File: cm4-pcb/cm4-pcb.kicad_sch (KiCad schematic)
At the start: 34 parts, among them J1 Conn_01x02_Pin, J2 Conn_01x02_Pin, J3 USB1125-GF-B, J4 Conn_02x03_Odd_Even, J5 Conn_01x04, J6 J0011D21NL, J7 Conn_01x02, U1 Pfostenstecker_6_2x3, U2 Pfostenstecker_6_2x3, U5 SMD-PUSH-BTN

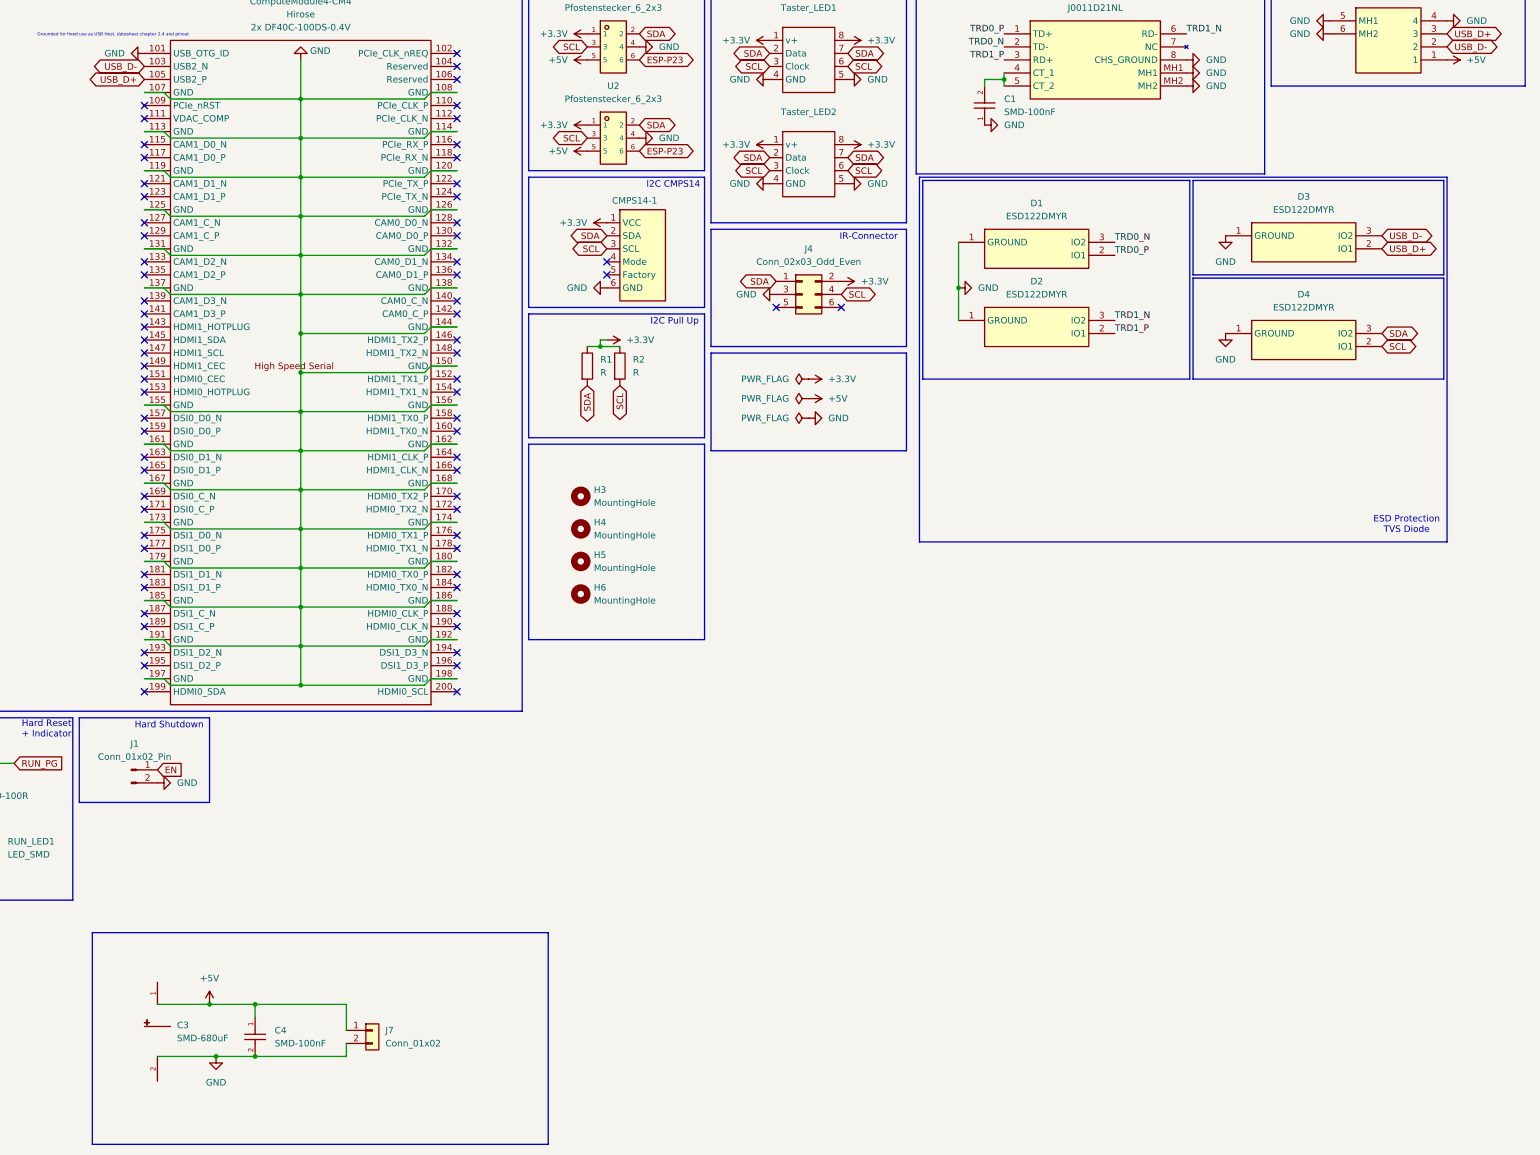
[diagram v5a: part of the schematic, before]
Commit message: Added 5v Connector
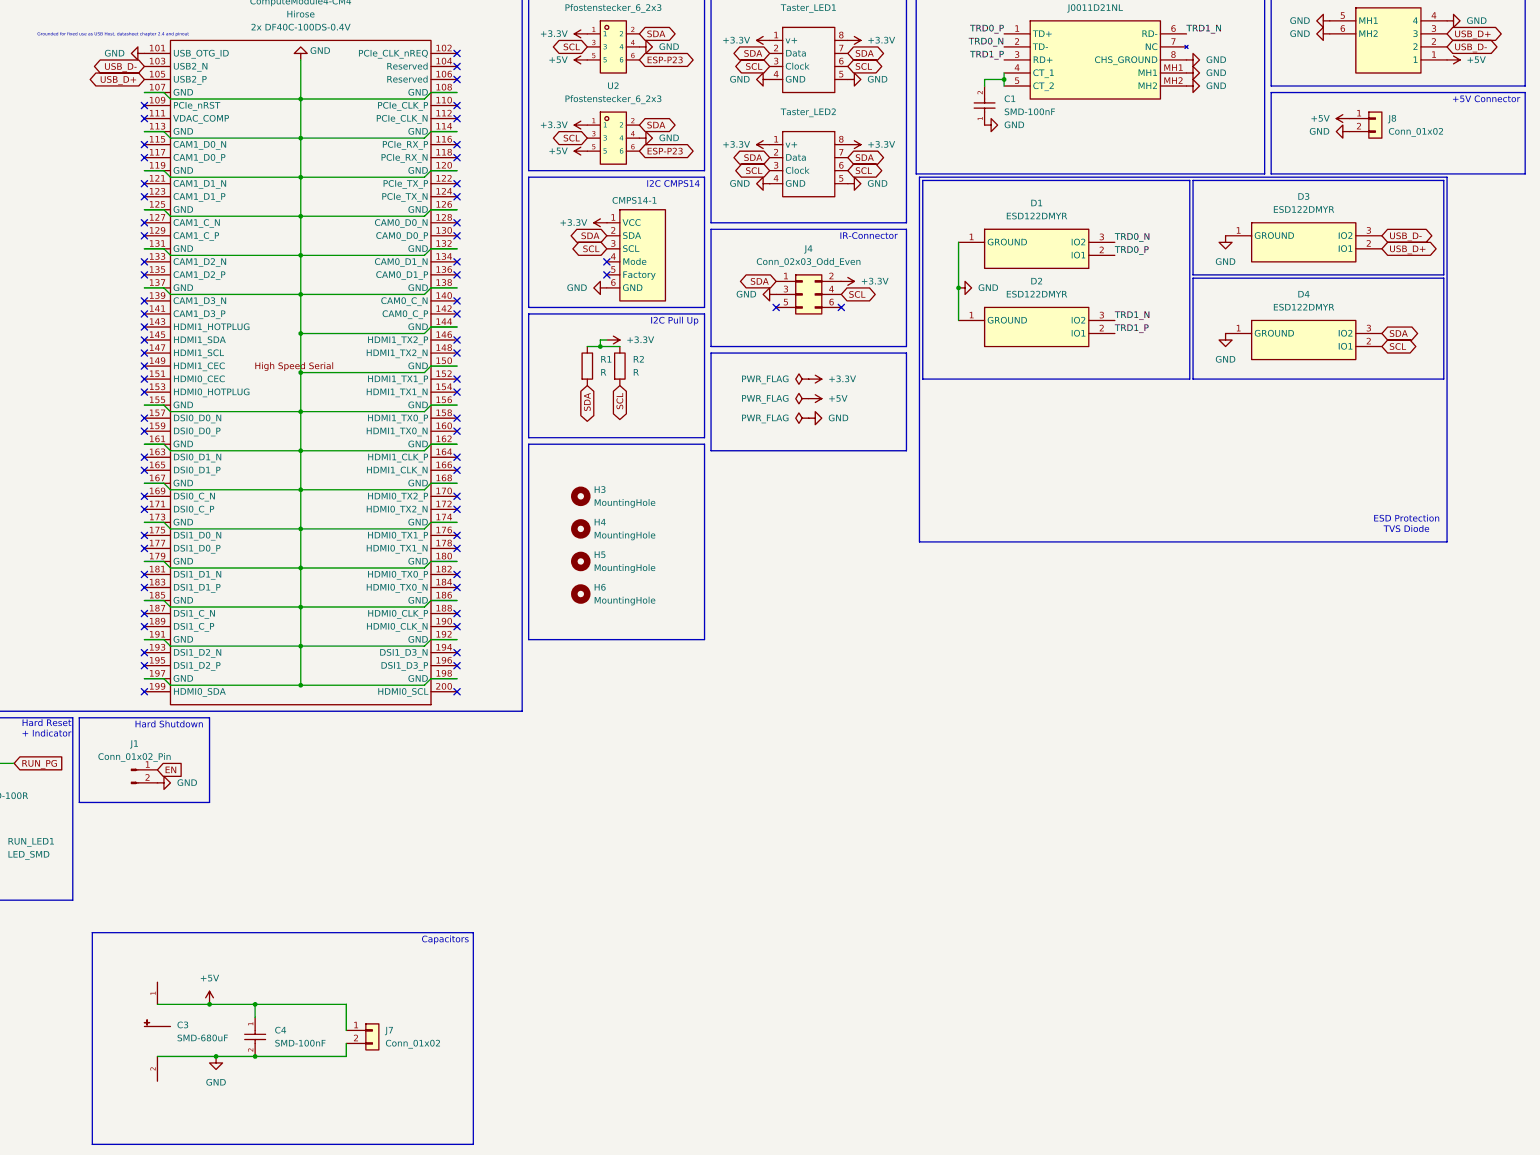
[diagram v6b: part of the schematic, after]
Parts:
- added J8: Conn_01x02, Connector_PinHeader_2.54mm:PinHeader_1x02_P2.54mm_Vertical, symbol Connector_Generic:Conn_01x02
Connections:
- net +5V: now also J8.1 (Pin_1)
- net GND: now also J8.2 (Pin_2)
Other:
- note added: "+5V Connector"
- note added: "Capacitors"
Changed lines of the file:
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@@
 	)
 	(rectangle
+		(start 349.25 35.56)
+		(end 398.78 51.435)
+		(stroke
+			(width 0)
+			(type default)
+		)
+		(fill
+			(type none)
+		)
+	)
+	(rectangle
 		(start 12.7 157.48)
 		(end 76.2 193.04)
@@
 	(rectangle
 		(start 119.38 199.39)
-		(end 208.28 240.665)
+		(end 193.675 240.665)
 		(stroke
 			(width 0)
@@
 		)
 	)
+	(text "+5V Connector"
+		(exclude_from_sim no)
+		(at 391.16 37.084 0)
+		(effects
+			(font
+				(size 1.27 1.27)
+			)
+		)
+	)
 	(text "IR-Connector"
 		(exclude_from_sim no)
@@
 		)
 	)
+	(text "Capacitors"
+		(exclude_from_sim no)
+		(at 188.214 200.914 0)
+		(effects
+			(font
+				(size 1.27 1.27)
+			)
+		)
+	)
 	(text "CM4\n"
 		(exclude_from_sim no)
@@
 	)
 	(symbol
+		(lib_id "Connector_Generic:Conn_01x02")
+		(at 369.57 40.64 0)
+		(unit 1)
+		(exclude_from_sim no)
+		(in_bom yes)
+		(on_board yes)
+		(dnp no)
+		(fields_autoplaced yes)
+		(property "Reference" "J8"
+			(at 372.11 40.6399 0)
+			(effects
+				(font
+					(size 1.27 1.27)
+				)
+				(justify left)
+			)
+		)
+		(property "Value" "Conn_01x02"
+			(at 372.11 43.1799 0)
+			(effects
+				(font
+					(size 1.27 1.27)
+				)
+				(justify left)
+			)
+		)
+		(property "Footprint" "Connector_PinHeader_2.54mm:PinHeader_1x02_P2.54mm_Vertical"
+			(at 369.57 40.64 0)
+			(effects
+				(font
+					(size 1.27 1.27)
+				)
+				(hide yes)
+			)
+		)
+		(property "Datasheet" "~"
+			(at 369.57 40.64 0)
+			(effects
+				(font
+					(size 1.27 1.27)
+				)
+				(hide yes)
+			)
+		)
+		(property "Description" "Generic connector, single row, 01x02, script generated (kicad-library-utils/schlib/autogen/connector/)"
+			(at 369.57 40.64 0)
+			(effects
+				(font
+					(size 1.27 1.27)
+				)
+				(hide yes)
+			)
+		)
+		(pin "1"
+		)
+		(pin "2"
+		)
+		(instances
+			(project "cm4-pcb"
+				(path "/498e70b5-f2fd-4a95-9aba-8c3678ffa14c"
+					(reference "J8")
+					(unit 1)
+				)
+			)
+		)
+	)
+	(symbol
 		(lib_id "bohlebots.lib:Taster_Led")
 		(at 260.35 25.4 0)
@@
 	)
 	(symbol
+		(lib_id "bohlebots.lib:GND")
+		(at 364.49 43.18 270)
+		(unit 1)
+		(exclude_from_sim no)
+		(in_bom yes)
+		(on_board yes)
+		(dnp no)
+		(fields_autoplaced yes)
+		(property "Reference" "#PWR046"
+			(at 358.14 43.18 0)
+			(effects
+				(font
+					(size 1.27 1.27)
+				)
+				(hide yes)
+			)
+		)
+		(property "Value" "GND"
+			(at 360.68 43.1799 90)
+			(effects
+				(font
+					(size 1.27 1.27)
+				)
+				(justify right)
+			)
+		)
+		(property "Footprint" ""
+			(at 364.49 43.18 0)
+			(effects
+				(font
+					(size 1.27 1.27)
+				)
+				(hide yes)
+			)
+		)
+		(property "Datasheet" ""
+			(at 364.49 43.18 0)
+			(effects
+				(font
+					(size 1.27 1.27)
+				)
+				(hide yes)
+			)
+		)
+		(property "Description" "Power symbol creates a global label with name \"GND\" , ground"
+			(at 364.49 43.18 0)
+			(effects
+				(font
+					(size 1.27 1.27)
+				)
+				(hide yes)
+			)
+		)
+		(pin "1"
+		)
+		(instances
+			(project "cm4-pcb"
+				(path "/498e70b5-f2fd-4a95-9aba-8c3678ffa14c"
+					(reference "#PWR046")
+					(unit 1)
+				)
+			)
+		)
+	)
+	(symbol
 		(lib_id "bohlebots.lib:MountingHole")
 		(at 214.63 133.35 0)
@@
 					(unit 1)
 				)
+			)
+		)
+	)
+	(symbol
+		(lib_id "bohlebots.lib:+5V")
+		(at 364.49 40.64 90)
+		(unit 1)
+		(exclude_from_sim no)
+		(in_bom yes)
+		(on_board yes)
+		(dnp no)
+		(fields_autoplaced yes)
+		(property "Reference" "#PWR038"
+			(at 368.3 40.64 0)
+			(effects
+				(font
+					(size 1.27 1.27)
+				)
+				(hide yes)
+			)
+		)
+		(property "Value" "+5V"
+			(at 360.68 40.6399 90)
+			(effects
+				(font
+					(size 1.27 1.27)
+				)
+				(justify left)
+			)
+		)
+		(property "Footprint" ""
+			(at 364.49 40.64 0)
+			(effects
+				(font
+					(size 1.27 1.27)
+				)
+				(hide yes)
+			)
+		)
+		(property "Datasheet" ""
+			(at 364.49 40.64 0)
+			(effects
+				(font
+					(size 1.27 1.27)
+				)
+				(hide yes)
+			)
+		)
+		(property "Description" "Power symbol creates a global label with name \"+5V\""
+			(at 364.49 40.64 0)
+			(effects
+				(font
+					(size 1.27 1.27)
+				)
+				(hide yes)
+			)
+		)
+		(pin "1"
+		)
+		(instances
+			(project "cm4-pcb"
+				(path "/498e70b5-f2fd-4a95-9aba-8c3678ffa14c"
+					(reference "#PWR038")
+					(unit 1)
+				)
